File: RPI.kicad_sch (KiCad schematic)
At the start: 28 parts, among them J1 Conn_01x02_Male, J2 GPIO, J5 Conn_01x06, J6 Conn_01x04, J7 Conn_01x03, J8 Conn_01x02, J9 Conn_01x02, Q1 IRF9540N, Q2 IRF9540N, Q3 BC856BDW1, SW1 SW_SPDT, SW2 SW_SPDT, U1 LM1085-ADJ

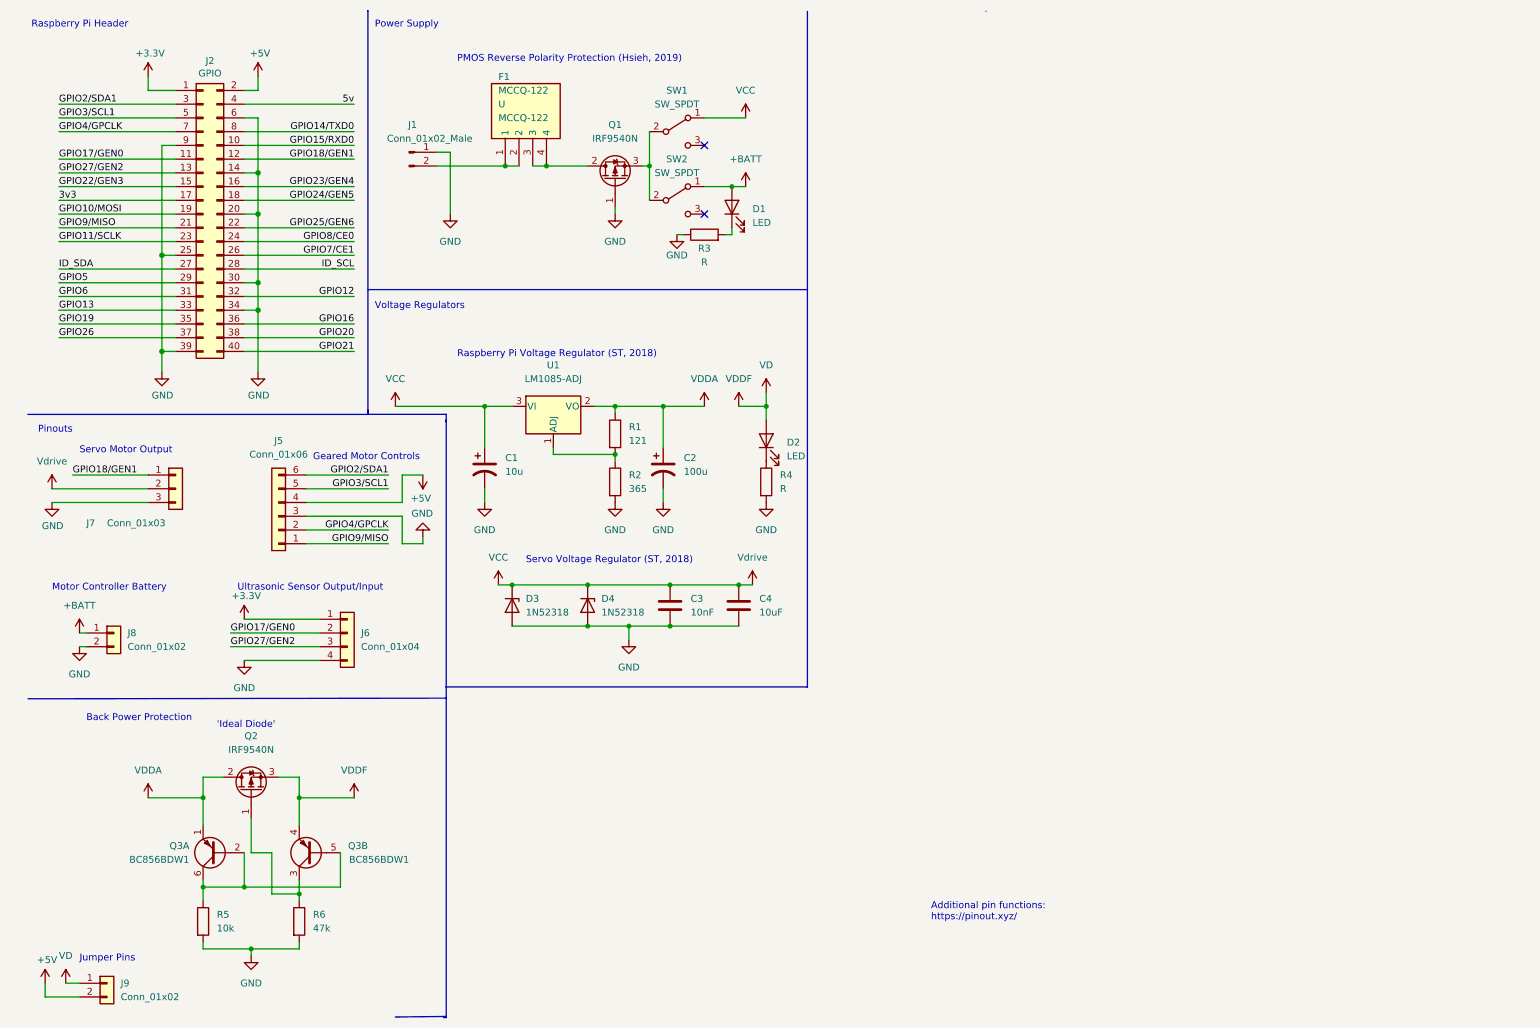
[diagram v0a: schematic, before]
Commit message: V2 Overhaul with new circuits and GPIO routes
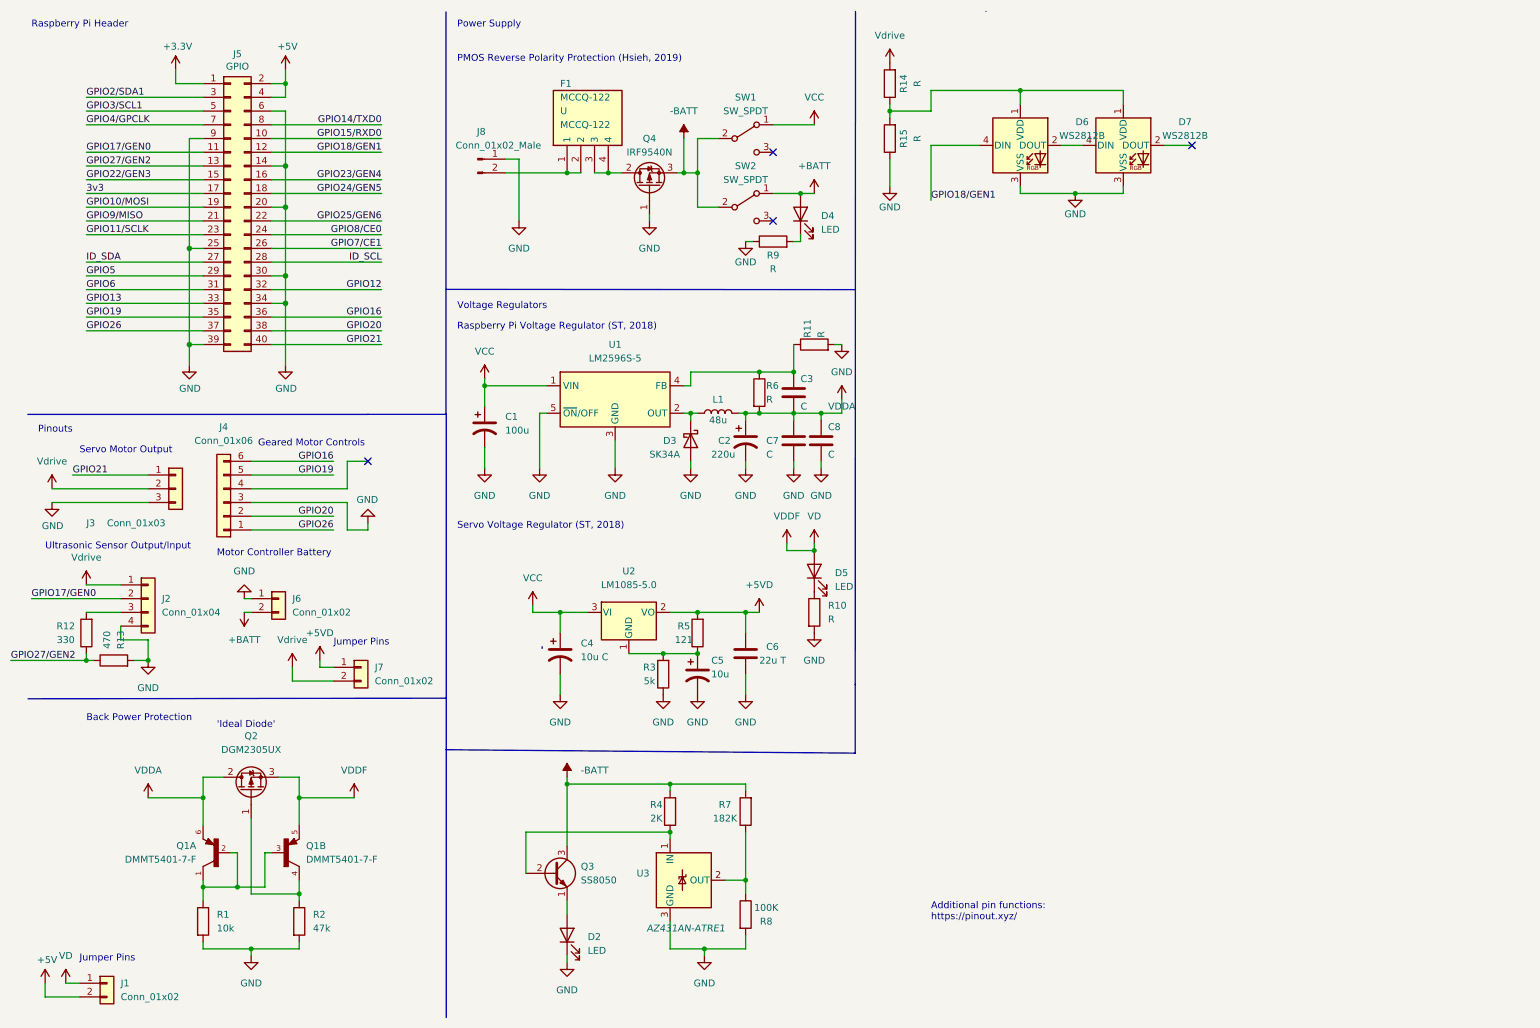
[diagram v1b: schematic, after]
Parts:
- removed C4: 10uF, Capacitor_SMD:C_0805_2012Metric_Pad1.18x1.45mm_HandSolder, symbol Device:C
- removed D3, D4: 1N52318, Diode_THT:D_DO-35_SOD27_P7.62mm_Horizontal, symbol Device:D_Zener
- removed Q3: BC856BDW1, Package_TO_SOT_SMD:SOT-363_SC-70-6, symbol Transistor_BJT:BC856BDW1
- removed R1: 121, Resistor_SMD:R_0805_2012Metric_Pad1.20x1.40mm_HandSolder, symbol Device:R
- removed R2: 365, Resistor_SMD:R_0805_2012Metric_Pad1.20x1.40mm_HandSolder, symbol Device:R
- removed U1: LM1085-ADJ, RPi_Hat:LM1085-5.0, symbol Regulator_Linear:LM1085-ADJ
- added C4: 10u C, Capacitor_SMD:C_0805_2012Metric_Pad1.18x1.45mm_HandSolder, symbol Device:C_Polarized_US
- added C5: 10u, Capacitor_SMD:C_0805_2012Metric_Pad1.18x1.45mm_HandSolder, symbol Device:C_Polarized_US
- added C6: 22u T, Capacitor_SMD:C_0805_2012Metric_Pad1.18x1.45mm_HandSolder, symbol Device:C
- added C7: C, Capacitor_SMD:C_0805_2012Metric_Pad1.18x1.45mm_HandSolder, symbol Device:C
- added C8: C, Capacitor_THT:CP_Radial_D5.0mm_P2.50mm, symbol Device:C
- added D2: LED, Diode_SMD:D_0805_2012Metric_Pad1.15x1.40mm_HandSolder, symbol Device:LED
- added D3: SK34A, Diode_SMD:D_SMA_Handsoldering, symbol Device:D_Schottky
- added D6, D7: WS2812B, LED_SMD:LED_WS2812B_PLCC4_5.0x5.0mm_P3.2mm, symbol LED:WS2812B
- added J7: Conn_01x02, Connector_PinSocket_2.54mm:PinSocket_1x02_P2.54mm_Vertical, symbol Connector_Generic:Conn_01x02
- added L1: 48u, Inductor_SMD:L_Bourns_SRR1260, symbol Device:L
- added Q1: DMMT5401-7-F, Package_TO_SOT_SMD:SOT-23-6_Handsoldering, symbol DMMT5401-7-F:DMMT5401-7-F
- added Q3: SS8050, Package_TO_SOT_SMD:SOT-23-3, symbol Transistor_BJT:S8050
- added R11, R14, R15, R6: R, Resistor_SMD:R_0805_2012Metric_Pad1.20x1.40mm_HandSolder, symbol Device:R
- added R12: 330, Resistor_SMD:R_0805_2012Metric_Pad1.20x1.40mm_HandSolder, symbol Device:R
- added R13: 470, Resistor_SMD:R_0805_2012Metric_Pad1.20x1.40mm_HandSolder, symbol Device:R
- added R3: 5k, Resistor_SMD:R_0805_2012Metric_Pad1.20x1.40mm_HandSolder, symbol Device:R
- added R4: 2K, Resistor_SMD:R_0805_2012Metric_Pad1.20x1.40mm_HandSolder, symbol Device:R
- added R5: 121, Resistor_SMD:R_0805_2012Metric_Pad1.20x1.40mm_HandSolder, symbol Device:R
- added R7: 182K, Resistor_SMD:R_0805_2012Metric_Pad1.20x1.40mm_HandSolder, symbol Device:R
- added R8: 100K, Resistor_SMD:R_0805_2012Metric_Pad1.20x1.40mm_HandSolder, symbol Device:R
- added U1: LM2596S-5, Package_TO_SOT_SMD:TO-263-5_TabPin3, symbol Regulator_Switching:LM2596S-5
- added U2: LM1085-5.0, Package_TO_SOT_THT:TO-220-3_Vertical, symbol Regulator_Linear:LM1085-5.0
- added U3: AZ431AN-ATRE1, Package_TO_SOT_SMD:SOT-23-3, symbol Reference_Voltage:REF3020
- C1: value 10u -> 100u; footprint Capacitor_THT:CP_Radial_D5.0mm_P2.50mm -> Capacitor_SMD:C_0805_2012Metric_Pad1.18x1.45mm_HandSolder
- C2: value 100u -> 220u; footprint Capacitor_Tantalum_SMD:CP_EIA-2012-12_Kemet-R_Pad1.30x1.05mm_HandSolder -> Capacitor_SMD:C_0805_2012Metric_Pad1.18x1.45mm_HandSolder
- C3: value 10nF -> C
- J6: renamed from J8; footprint Connector_PinSocket_2.54mm:PinSocket_1x02_P2.54mm_Vertical -> RPi_Hat:TE_282836-2
- Q2: value IRF9540N -> DGM2305UX; footprint Package_TO_SOT_THT:TO-220-3_Vertical -> Package_TO_SOT_SMD:SOT-23
- renumbered D1 to D4, D2 to D5, J9 to J1, J6 to J2, J7 to J3, J5 to J4, J2 to J5, J1 to J8, Q1 to Q4, R5 to R1, R4 to R10, R6 to R2, R3 to R9
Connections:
- net 5v is gone; now on net +5V: J5.4 (Pin_4)
- net +3V3: no longer J2.1 (Pin_1)
- net +5V: no longer J4.4 (Pin_4)
- net +BATT: now also J6.2 (Pin_2); no longer J6.1 (Pin_1)
- net GND: now also J6.1 (Pin_1), C4.2, C5.2, C6.2, C7.2, C8.2, D2.1 (K), D3.2 (A), D6.3 (VSS), D7.3 (VSS), R11.2, R13.2, R15.1, R3.1, R8.2, U1.3 (GND), U1.5 (~{ON}/OFF), U3.3 (GND); no longer C3.2, J6.2 (Pin_2)
- net GPIO16: now also J4.6 (Pin_6)
- net GPIO18/GEN1: now also D6.4 (DIN); no longer J3.1 (Pin_1)
- net GPIO19: now also J4.5 (Pin_5)
- net GPIO20: now also J4.2 (Pin_2)
- net GPIO21: now also J3.1 (Pin_1)
- net GPIO26: now also J4.1 (Pin_1)
- net GPIO27/GEN2: now also R12.1, R13.1; no longer J2.3 (Pin_3)
- net GPIO2/SDA1: no longer J4.6 (Pin_6)
- net GPIO3/SCL1: no longer J4.5 (Pin_5)
- net GPIO4/GPCLK: no longer J4.2 (Pin_2)
- net GPIO9/MISO: no longer J4.1 (Pin_1)
- net VCC: now also C4.1, U1.1 (VIN), U2.3 (VI); no longer C3.1, J3.2 (Pin_2)
- net VD: now also Q1.5
- net VDDA: now also C3.2, C7.1, C8.1, L1.2, Q1.6, R6.2
- net at R1.1: now also Q1.1, Q1.2, Q1.3
- net -BATT: now reaches Q4.3 (S), SW1.2 (B), SW2.2 (B)
- net -BATT: now also Q3.3 (C), R4.2, R7.2
- net at Q2.1 (G), R2.1: now also Q1.4
- new net: J2.3 (Pin_3), R12.2
- new net: D6.1 (VDD), D7.1 (VDD), R14.1, R15.2
- new net: D2.2 (A), Q3.1 (E)
- new net: Q3.2 (B), R4.1, U3.1 (IN)
- new net: C5.1, R3.2, R5.1, U2.1 (GND)
- new net: R7.1, R8.1, U3.2 (OUT)
- new net: D6.2 (DOUT), D7.4 (DIN)
- new net: C3.1, R11.1, R6.1, U1.4 (FB)
- new net: D3.1 (K), L1.1, U1.2 (OUT)
- new net +5VD: C6.1, J7.1 (Pin_1), R5.2, U2.2 (VO)
- new net Vdrive: J2.1 (Pin_1), J3.2 (Pin_2), J7.2 (Pin_2), R14.2
- no-connect marks 2 -> 4
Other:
- moved on the sheet: D4, D5, F1, J2, J4, J5, J6, J8, Q4, R10, R9, SW1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

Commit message: Added via stitching and titles
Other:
- added sheet buck reg (test.kicad_sch)
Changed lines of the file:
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@@
     (pin "2")
+  )
+  (sheet (at 201.93 111.76) (size 31.75 22.86) (fields_autoplaced)
+    (stroke (width 0.1524) (type solid) (color 0 0 0 0))
+    (fill (color 0 0 0 0.0000))
+    (property "Sheet name" "buck reg" (id 0) (at 201.93 111.0484 0)
+      (effects (font (size 1.27 1.27)) (justify left bottom))
+    )
+    (property "Sheet file" "test.kicad_sch" (id 1) (at 201.93 135.2046 0)
+      (effects (font (size 1.27 1.27)) (justify left top))
+    )
   )
   (sheet_instances
     (path "/" (page "1"))
+    (path "/bf1e2c51-a642-47c0-94b6-9f1533755b50" (page "2"))
   )
   (symbol_instances

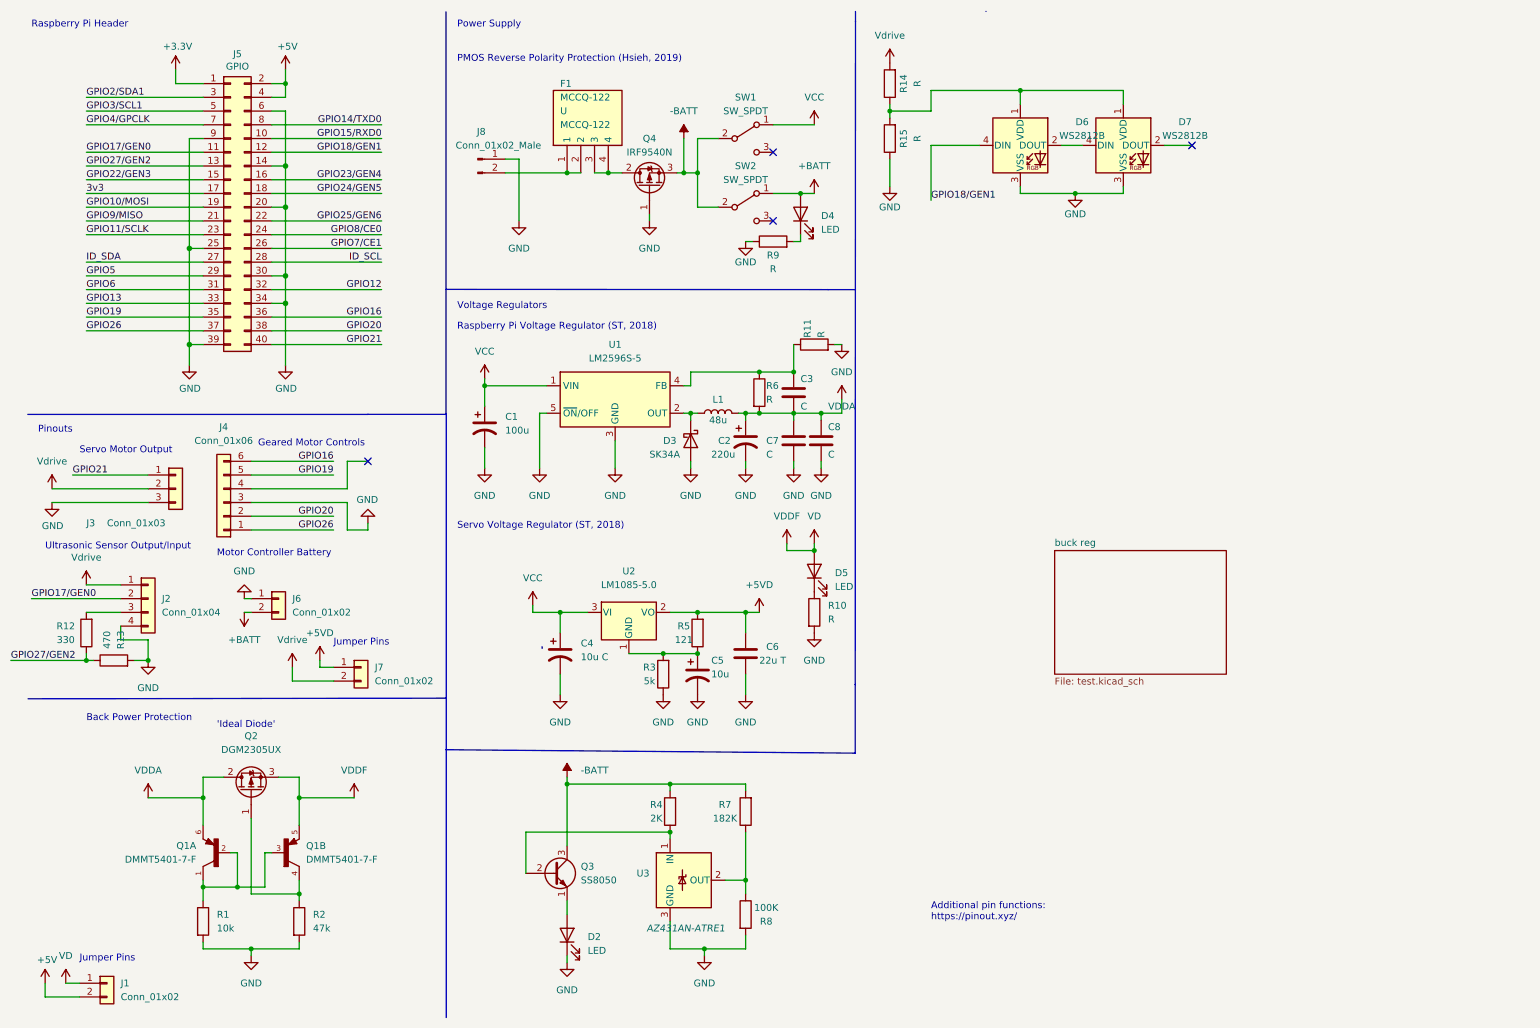
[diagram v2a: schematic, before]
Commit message: Updated Schematic & finalised PCB design
- Schematic more readable
- Finalised silkscreen
- Generate Gerber
- Cleaned Folder structure
- Added missing 3D models
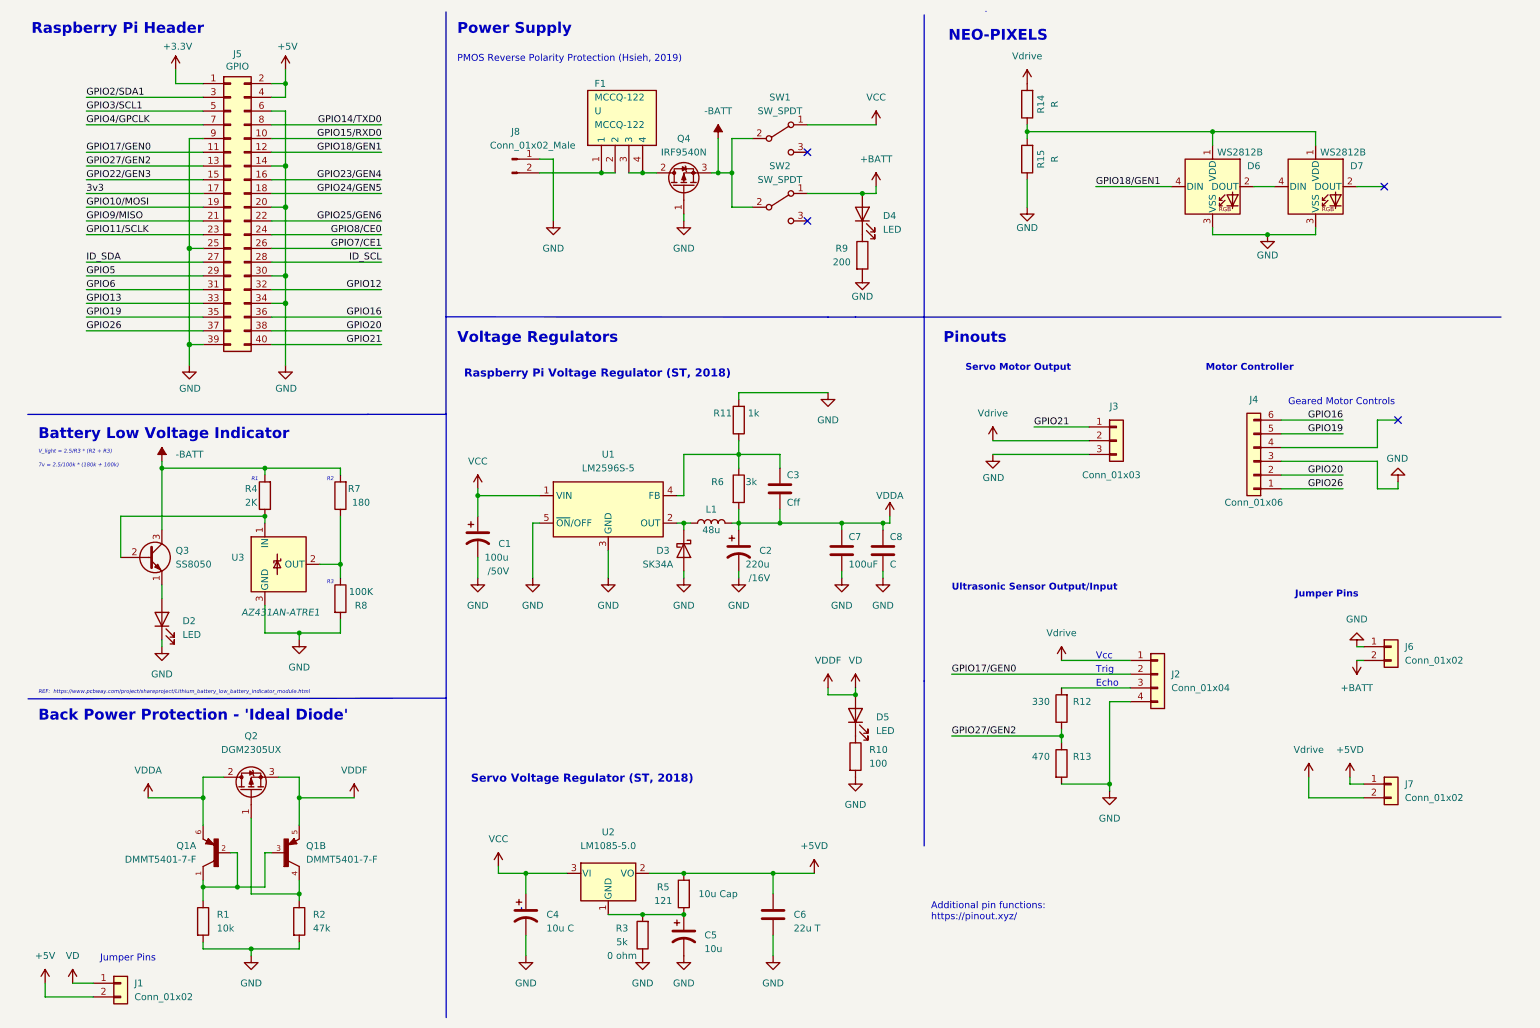
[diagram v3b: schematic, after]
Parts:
- C1: Voltage (none) -> /50V
- C2: Voltage (none) -> /16V
- C3: value C -> Cff
- C7: value C -> 100uF
- R10: value R -> 100
- R11: value R -> 1k
- R3: Option (none) -> 0 ohm
- R5: Option (none) -> 10u Cap
- R6: value R -> 3k
- R7: value 182K -> 180
- R9: value R -> 200
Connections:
- net GND: now also R9.2; no longer R9.1
- net at D4.1 (K): now also R9.1; no longer R9.2
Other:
- removed sheet buck reg
- note added: "7v = 2.5/100k * (180k + 100k)"
- note added: "Back Power Protection - 'Ideal Diode'"
- note added: "Battery Low Voltage Indicator"
- note added: "Echo"
- note added: "Motor Controller"
- note added: "NEO-PIXELS"
- note added: "R1"
- note added: "R2"
- note added: "R3"
- note added: "REF: https://www.pcbway.com/project/shareproject/Lithium_battery_low_battery_indicator_module.html"
- note added: "Trig"
- note added: "V_light = 2.5/R3 * (R2 + R3)"
- note added: "Vcc"
- note removed: "'Ideal Diode'"
- note removed: "Back Power Protection"
- note removed: "Motor Controller Battery"
- moved on the sheet: C1, C2, C3, C4, C5, C6, C7, C8, D2, D3, D4, D5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

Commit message: Slight placement adjustment of schematic
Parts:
- R3: value 5k -> 365
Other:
- moved on the sheet: C1, C2, C3, C4, C5, C6, C7, C8, D3, D5, L1, R10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

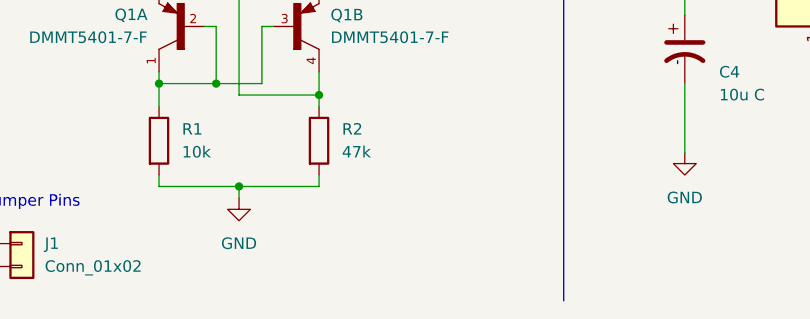
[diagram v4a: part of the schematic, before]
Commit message: added ref to Ideal diode
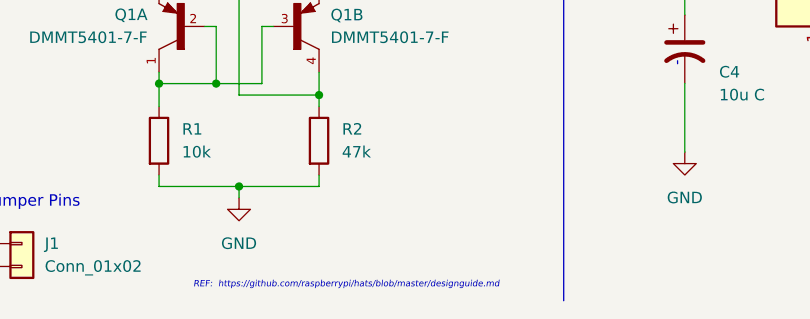
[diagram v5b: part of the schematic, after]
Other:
- note added: "REF: https://github.com/raspberrypi/hats/blob/master/designguide.md"
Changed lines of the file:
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@@
     (stroke (width 0) (type default) (color 0 0 0 0))
+  )
+  (text "REF:  https://github.com/raspberrypi/hats/blob/master/designguide.md"
+    (at 48.26 196.85 0)
+    (effects (font (size 0.7 0.7) italic) (justify left bottom))
   )
   (text "Battery Low Voltage Indicator" (at 13.97 91.44 0)

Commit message: Minor
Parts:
- C1: Voltage /50V -> /30V~
- C2: value 220u -> 47u; Voltage /16V -> /10V
- C7: value 100uF -> 47u; Voltage (none) -> /10v
- C8: value C -> 300u; Voltage (none) -> /10v
- R12: Alt (none) -> 1k
- R13: Alt (none) -> 2k
- R14: value R -> 1k
- R15: value R -> 2k
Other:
- note added: "Logic shift to 3.3v for pi"
- moved on the sheet: C2, C3, C7, R11, R6
